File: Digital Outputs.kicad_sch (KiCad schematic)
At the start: 14 parts, among them K1 RT214024, K2 RT214024, K3 RT214024, K4 RT214024, K5 RT214024, K6 RT214024, K7 RT214024, K8 RT214024, Q1 2N3904, Q2 2N3904, U1 ULN2003

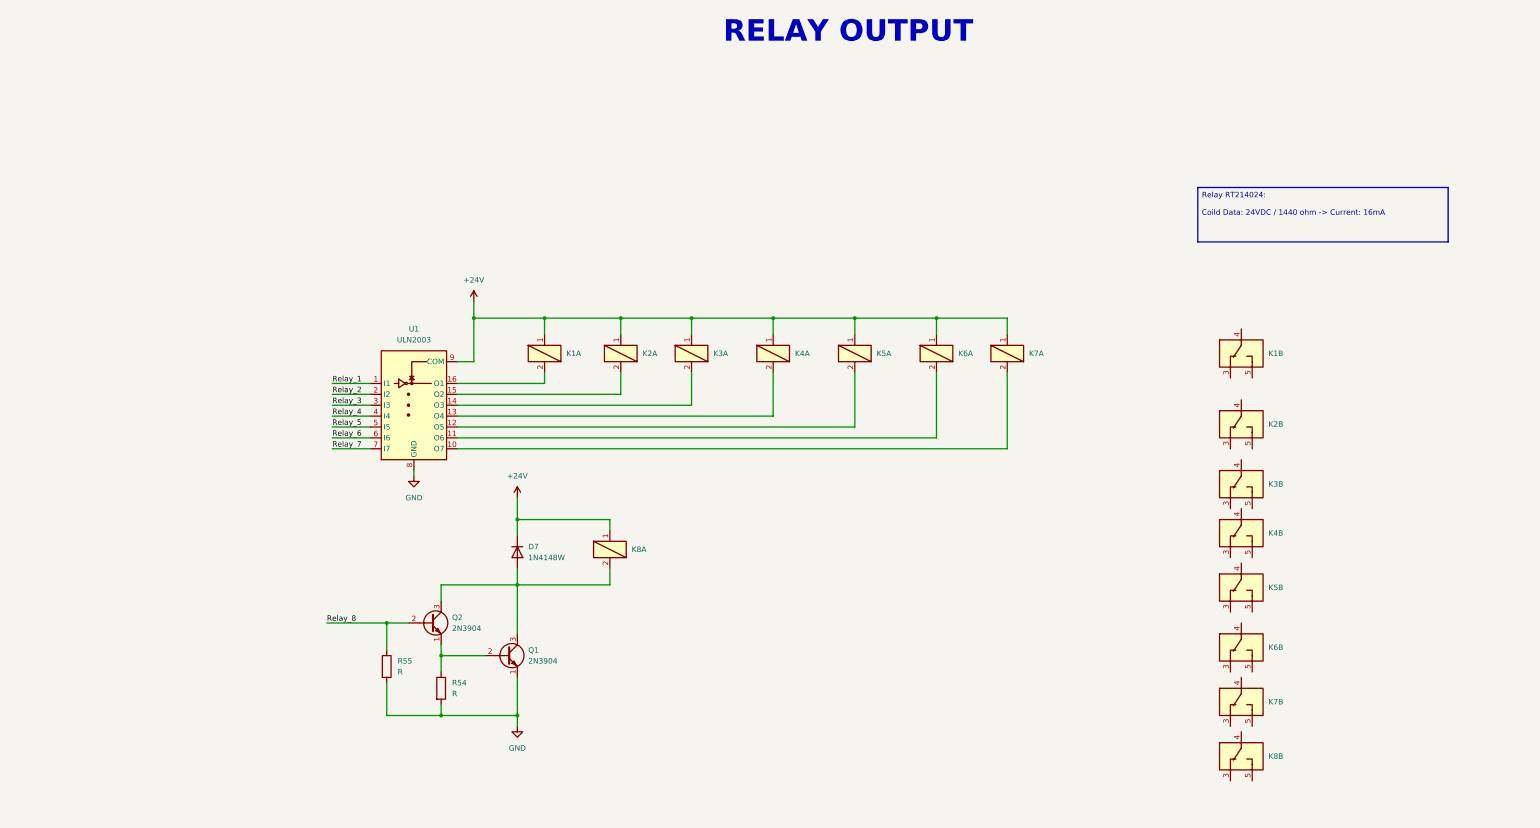
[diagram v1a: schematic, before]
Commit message: Se termina el circuito de entrada análoga, se escoge la bornera. Se termina las salidas de rele, se asumen que se trabajara maximo a 220V y solo para activar contactores. El circuito para el sensor namur se esta realizando
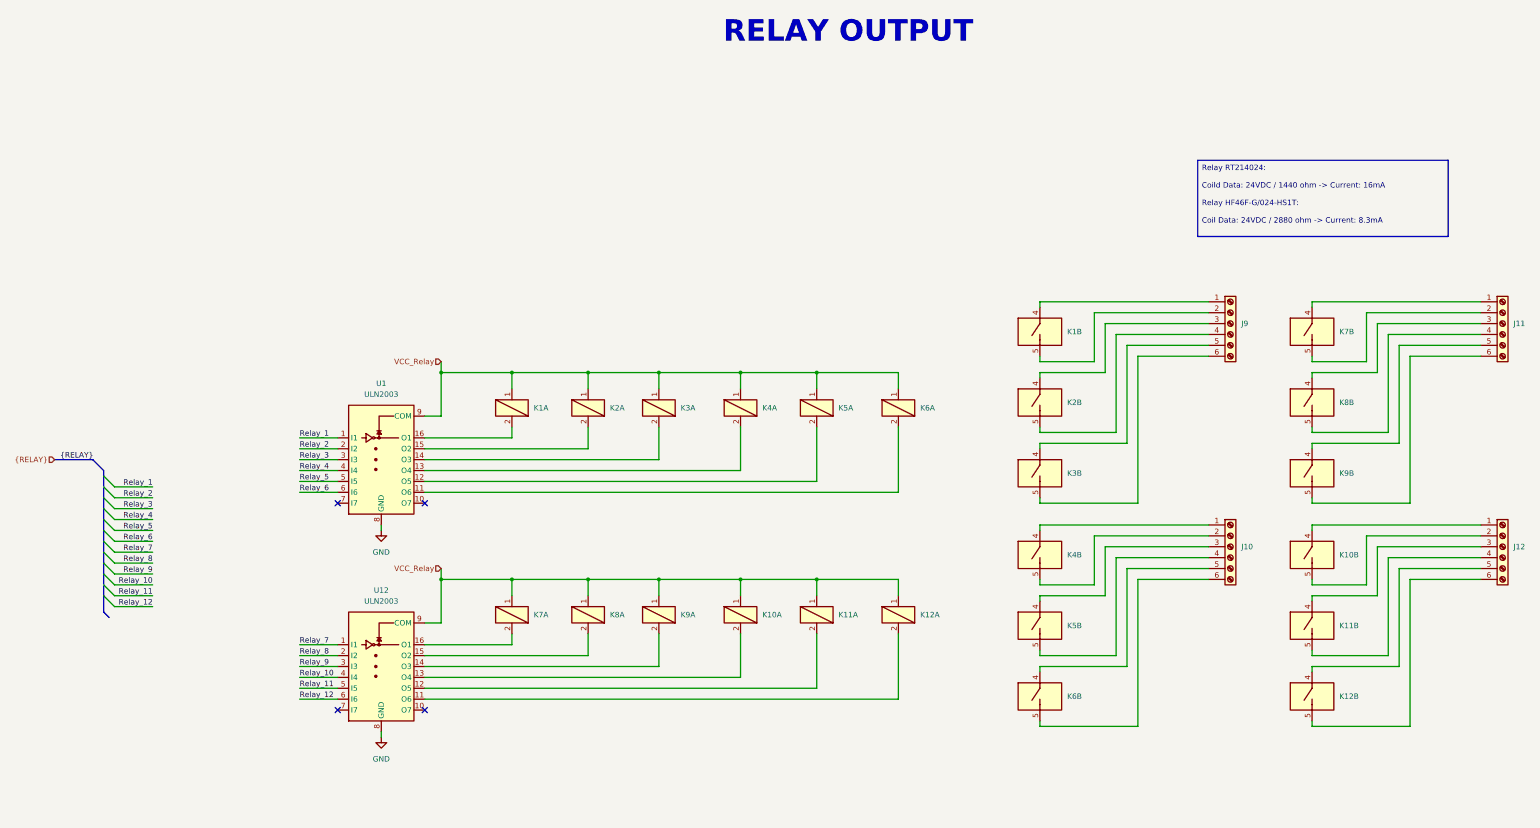
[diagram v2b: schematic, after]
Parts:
- removed D7: 1N4148W, Diode_SMD:D_SOD-123, symbol Diode:1N4148W
- removed K1, K2, K3, K4, K5, K6, K7, K8: RT214024, LIB_PCB_CONT:RT214024_TE-Connectivity, symbol LIB_SCH_CONTR:RT214024_TE-Connectivity
- removed Q1, Q2: 2N3904, Package_TO_SOT_THT:TO-92_Inline, symbol Transistor_BJT:2N3904
- removed R54, R55: R, symbol Device:R
- added J10, J11, J12, J9: Screw_Terminal_01x06, LIB_PCB_CONT:15EDGRC_6P_3.81mm_Male-Rect_Degson, symbol Connector:Screw_Terminal_01x06
- added K1, K10, K11, K12, K2, K3, K4, K5, K6, K7, K8, K9: HF46F-G, LIB_PCB_CONT:Relay_HF46F-G_Hongfa, symbol LIB_SCH_CONTR:HF46F-G_Hongfa
- added U12: ULN2003, 1-Package_SO:SOIC-16_3.9x9.9mm_P1.27mm, symbol 1-IC-General:ULN2003
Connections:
- net GND: now also U12.8 (GND)
- net Relay_7: now also U12.1 (I1); no longer U1.7 (I7)
- net Relay_8: now also U12.2 (I2)
- net at U1.12 (O5): now also K5.2
- net at U1.14 (O3): now also K3.2
- net at U1.11 (O6): now also K6.2
- net at U1.13 (O4): now also K4.2
- net at U1.15 (O2): now also K2.2
- net at U1.16 (O1): now also K1.2
- net +24V renamed VCC_Relay
- net VCC_Relay: now also K1.1, K10.1, K11.1, K12.1, K2.1, K3.1, K4.1, K5.1, K6.1, K7.1, K8.1, K9.1, U12.9 (COM)
- new net: K8.2, U12.15 (O2)
- new net: J10.3 (Pin_3), K5.4 (COM)
- new net: J10.4 (Pin_4), K5.5 (NO)
- new net: K9.2, U12.14 (O3)
- new net: J12.5 (Pin_5), K12.4 (COM)
- new net: J12.6 (Pin_6), K12.5 (NO)
- new net: J11.1 (Pin_1), K7.4 (COM)
- new net: J11.2 (Pin_2), K7.5 (NO)
- new net: J11.3 (Pin_3), K8.4 (COM)
- new net: J11.4 (Pin_4), K8.5 (NO)
- new net: J11.5 (Pin_5), K9.4 (COM)
- new net: J11.6 (Pin_6), K9.5 (NO)
- new net: J9.3 (Pin_3), K2.4 (COM)
- new net: J9.4 (Pin_4), K2.5 (NO)
- new net: J12.3 (Pin_3), K11.4 (COM)
- new net: J12.4 (Pin_4), K11.5 (NO)
- new net: K10.2, U12.13 (O4)
- new net: J10.5 (Pin_5), K6.4 (COM)
- new net: J10.6 (Pin_6), K6.5 (NO)
- new net: J9.5 (Pin_5), K3.4 (COM)
- new net: J9.6 (Pin_6), K3.5 (NO)
- new net: J9.1 (Pin_1), K1.4 (COM)
- new net: J9.2 (Pin_2), K1.5 (NO)
- new net: K12.2, U12.11 (O6)
- new net: K11.2, U12.12 (O5)
- new net: J10.1 (Pin_1), K4.4 (COM)
- new net: J10.2 (Pin_2), K4.5 (NO)
- new net: K7.2, U12.16 (O1)
- new net: J12.1 (Pin_1), K10.4 (COM)
- new net: J12.2 (Pin_2), K10.5 (NO)
- new net Relay_10: U12.4 (I4)
- new net Relay_11: U12.5 (I5)
- new net Relay_12: U12.6 (I6)
- new net Relay_9: U12.3 (I3)
- no-connect marks 0 -> 4
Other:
- moved on the sheet: U1

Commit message: Avance
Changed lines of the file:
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@@
 		)
 	)
-	(text_box "Relay RT214024:\n\nCoild Data: 24VDC / 1440 ohm -> Current: 16mA\n\nRelay HF46F-G/024-HS1T:\n\nCoil Data: 24VDC / 2880 ohm -> Current: 8.3mA"
+	(text_box "Relay RT214024:\n\nCoild Data: 24VDC / 1440 ohm -> Current: 16mA\n\nRelay HF46F-G/024-HS1T:\n\nCoil Data: 24VDC / 2880 ohm -> Current: 8.3mA\n\nRelay HF46F-G/012-HS1T:\n\nCoil Data: 12VDC / 720 ohm -> Current: 16.67mA"
 		(exclude_from_sim no)
-		(at 290.83 63.5 0)
-		(size 58.42 17.78)
+		(at 278.13 54.61 0)
+		(size 58.42 26.67)
 		(margins 0.9525 0.9525 0.9525 0.9525)
 		(stroke

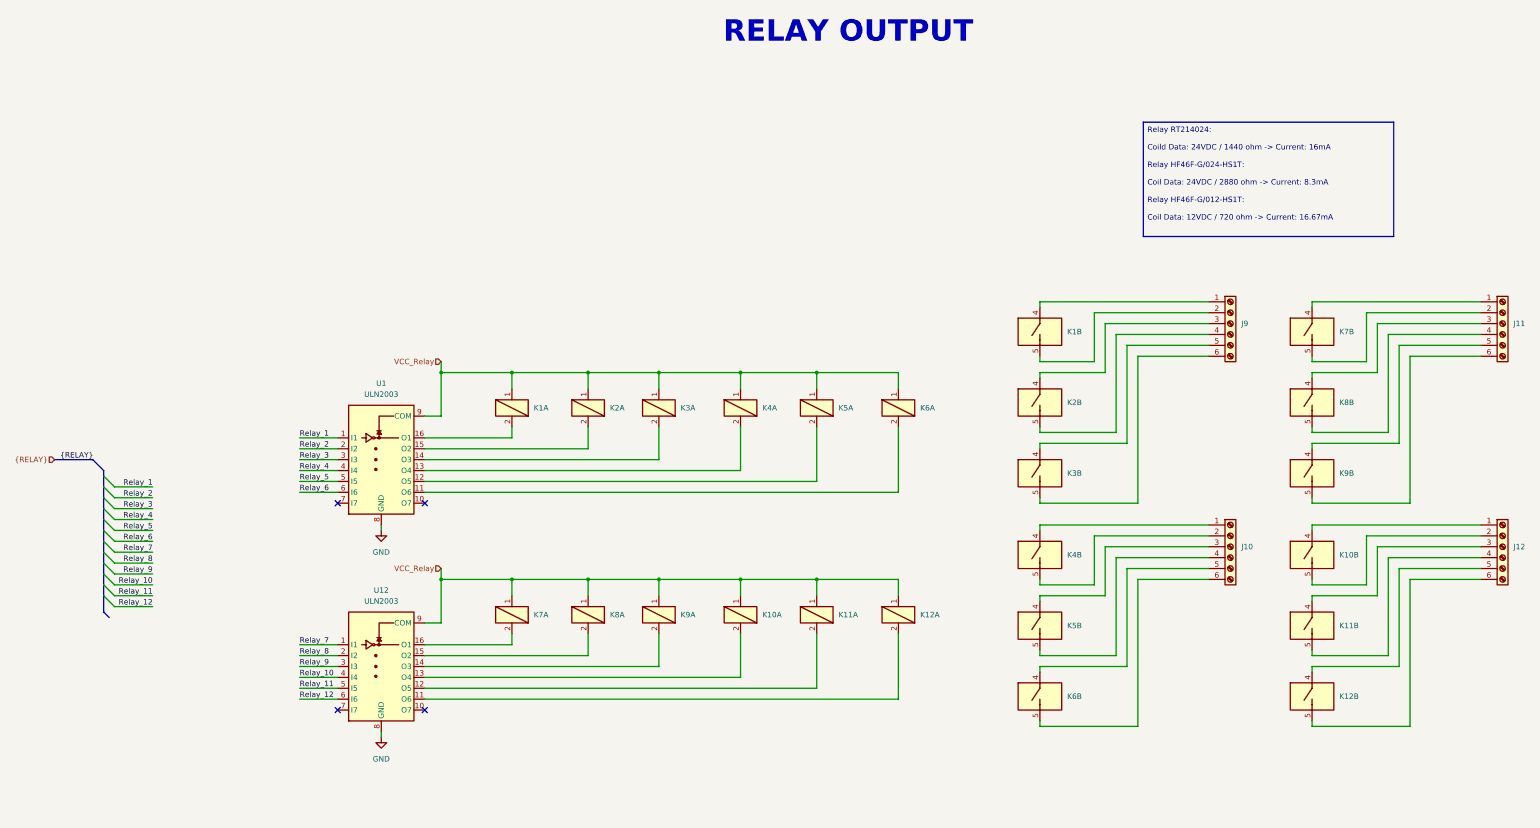
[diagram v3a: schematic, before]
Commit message: avance de pcb, se considera borneras externas para conexión de alimentación
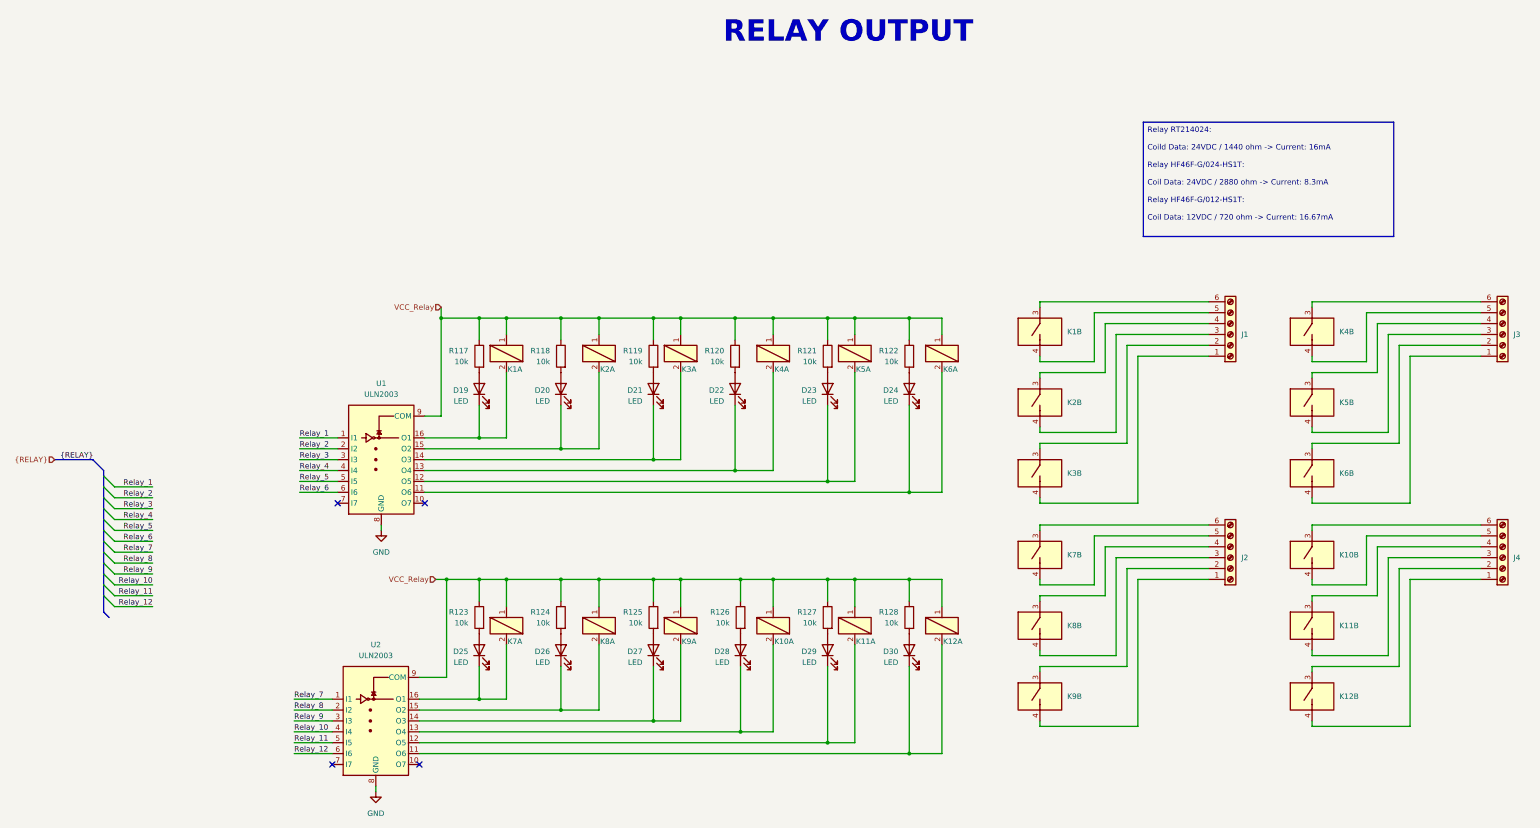
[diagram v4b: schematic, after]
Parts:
- removed unit 2 of K6
- removed unit 2 of K7
- added D19, D20, D21, D22, D23, D24, D25, D26, D27, D28, D29, D30: LED, LED_SMD:LED_0603_1608Metric, symbol Device:LED
- added unit 2 of K4
- added unit 2 of K9
- added R117, R118, R119, R120, R121, R122, R123, R124, R125, R126, R127, R128: 10k, Resistor_SMD:R_0603_1608Metric, symbol Device:R
- J1: renamed from J9; footprint LIB_PCB_CONT:15EDGRC_6P_3.81mm_Male-Rect_Degson -> LIB_PCB_CONT:15EDGVC_6P_3.81mm_Male-Vert_Degson
- J2: renamed from J10; footprint LIB_PCB_CONT:15EDGRC_6P_3.81mm_Male-Rect_Degson -> LIB_PCB_CONT:15EDGVC_6P_3.81mm_Male-Vert_Degson
- J3: renamed from J11; footprint LIB_PCB_CONT:15EDGRC_6P_3.81mm_Male-Rect_Degson -> LIB_PCB_CONT:15EDGVC_6P_3.81mm_Male-Vert_Degson
- J4: renamed from J12; footprint LIB_PCB_CONT:15EDGRC_6P_3.81mm_Male-Rect_Degson -> LIB_PCB_CONT:15EDGVC_6P_3.81mm_Male-Vert_Degson
- renumbered K9 to K6, K4 to K7, U12 to U2
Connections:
- net VCC_Relay: now also R117.1, R118.1, R119.1, R120.1, R121.1, R122.1, R123.1, R124.1, R125.1, R126.1, R127.1, R128.1
- net at K8.2, U2.15 (O2): now also D26.1 (K)
- net at K5.4 (NO): now also J3.3 (Pin_3); no longer J2.3 (Pin_3)
- net at J2.4 (Pin_4): now also K8.3 (COM); no longer K5.5 (NO)
- net at K9.2, U2.14 (O3): now also D27.1 (K)
- net at K1.2, U1.16 (O1): now also D19.1 (K)
- net at K12.4 (NO): now also J4.1 (Pin_1); no longer J4.5 (Pin_5)
- net at J4.6 (Pin_6): now also K10.3 (COM); no longer K12.5 (NO)
- net at J3.1 (Pin_1): now also K6.4 (NO)
- net at J3.2 (Pin_2): now also K6.3 (COM)
- net at K8.4 (NO): now also J2.3 (Pin_3); no longer J3.3 (Pin_3)
- net at J3.4 (Pin_4): now also K5.3 (COM); no longer K8.5 (NO)
- net at J3.5 (Pin_5): now also K4.4 (NO); no longer K6.4 (COM)
- net at J3.6 (Pin_6): now also K4.3 (COM); no longer K6.5 (NO)
- net at J1.4 (Pin_4): now also K2.3 (COM); no longer K2.5 (NO)
- net at K3.2, U1.14 (O3): now also D21.1 (K)
- net at J4.4 (Pin_4): now also K11.3 (COM); no longer K11.5 (NO)
- net at K10.2, U2.13 (O4): now also D28.1 (K)
- net at J2.5 (Pin_5): now also K7.4 (NO)
- net at J2.6 (Pin_6): now also K7.3 (COM)
- net at J1.5 (Pin_5): now also K1.4 (NO); no longer K3.4 (COM)
- net at J1.6 (Pin_6): now also K1.3 (COM); no longer K3.5 (NO)
- net at K4.2, U1.13 (O4): now also D22.1 (K)
- net at J1.1 (Pin_1): now also K3.4 (NO); no longer K1.4 (COM)
- net at J1.2 (Pin_2): now also K3.3 (COM); no longer K1.5 (NO)
- net at K12.2, U2.11 (O6): now also D30.1 (K)
- net at K6.2, U1.11 (O6): now also D24.1 (K)
- net at K5.2, U1.12 (O5): now also D23.1 (K)
- net at K2.2, U1.15 (O2): now also D20.1 (K)
- net at K11.2, U2.12 (O5): now also D29.1 (K)
- net at J2.1 (Pin_1): now also K9.4 (NO); no longer K7.4 (COM)
- net at J2.2 (Pin_2): now also K9.3 (COM); no longer K7.5 (NO)
- net at K7.2, U2.16 (O1): now also D25.1 (K)
- net at K10.4 (NO): now also J4.5 (Pin_5); no longer J4.1 (Pin_1)
- net at J4.2 (Pin_2): now also K12.3 (COM); no longer K10.5 (NO)
- new net: D29.2 (A), R127.2
- new net: D22.2 (A), R120.2
- new net: D30.2 (A), R128.2
- new net: D20.2 (A), R118.2
- new net: D21.2 (A), R119.2
- new net: D25.2 (A), R123.2
- new net: D27.2 (A), R125.2
- new net: D24.2 (A), R122.2
- new net: D26.2 (A), R124.2
- new net: D19.2 (A), R117.2
- new net: D28.2 (A), R126.2
- new net: D23.2 (A), R121.2
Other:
- moved on the sheet: K12A, K1A, U2

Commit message: Se añaden leds a la entrada de los Namur. Se estandariza y revisan varios footprints de los capacitores. El cambio no fue demasiado, se corrigio en placa. Se hacen algunos cambios adicionales a los valores. Se realiza un avance para jlcpcb
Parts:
- D19, D20, D21, D22, D23, D24, D25, D26, D27, D28, D29, D30: footprint LED_SMD:LED_0603_1608Metric -> LED_SMD:LED_0805_2012Metric
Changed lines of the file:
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@@
 			)
 		)
-		(property "Footprint" "LED_SMD:LED_0603_1608Metric"
+		(property "Footprint" "LED_SMD:LED_0805_2012Metric"
 			(at 182.88 116.84 0)
 			(effects
@@
 			)
 		)
-		(property "Footprint" "LED_SMD:LED_0603_1608Metric"
+		(property "Footprint" "LED_SMD:LED_0805_2012Metric"
 			(at 142.24 116.84 0)
 			(effects
@@
 			)
 		)
-		(property "Footprint" "LED_SMD:LED_0603_1608Metric"
+		(property "Footprint" "LED_SMD:LED_0805_2012Metric"
 			(at 163.83 116.84 0)
 			(effects
@@
 			)
 		)
-		(property "Footprint" "LED_SMD:LED_0603_1608Metric"
+		(property "Footprint" "LED_SMD:LED_0805_2012Metric"
 			(at 123.19 177.8 0)
 			(effects
@@
 			)
 		)
-		(property "Footprint" "LED_SMD:LED_0603_1608Metric"
+		(property "Footprint" "LED_SMD:LED_0805_2012Metric"
 			(at 163.83 177.8 0)
 			(effects
@@
 			)
 		)
-		(property "Footprint" "LED_SMD:LED_0603_1608Metric"
+		(property "Footprint" "LED_SMD:LED_0805_2012Metric"
 			(at 142.24 177.8 0)
 			(effects
@@
 			)
 		)
-		(property "Footprint" "LED_SMD:LED_0603_1608Metric"
+		(property "Footprint" "LED_SMD:LED_0805_2012Metric"
 			(at 123.19 116.84 0)
 			(effects
@@
 			)
 		)
-		(property "Footprint" "LED_SMD:LED_0603_1608Metric"
+		(property "Footprint" "LED_SMD:LED_0805_2012Metric"
 			(at 223.52 177.8 0)
 			(effects
@@
 			)
 		)
-		(property "Footprint" "LED_SMD:LED_0603_1608Metric"
+		(property "Footprint" "LED_SMD:LED_0805_2012Metric"
 			(at 204.47 116.84 0)
 			(effects
@@
 			)
 		)
-		(property "Footprint" "LED_SMD:LED_0603_1608Metric"
+		(property "Footprint" "LED_SMD:LED_0805_2012Metric"
 			(at 223.52 116.84 0)
 			(effects
@@
 			)
 		)
-		(property "Footprint" "LED_SMD:LED_0603_1608Metric"
+		(property "Footprint" "LED_SMD:LED_0805_2012Metric"
 			(at 184.15 177.8 0)
 			(effects
@@
 			)
 		)
-		(property "Footprint" "LED_SMD:LED_0603_1608Metric"
+		(property "Footprint" "LED_SMD:LED_0805_2012Metric"
 			(at 204.47 177.8 0)
 			(effects
